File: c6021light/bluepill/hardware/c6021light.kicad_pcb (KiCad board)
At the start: 2 copper layers, 100 x 50 mm, 73 parts, among them J1 Barrel_Jack_Switch, J10 Conn_01x02, J11 Conn_01x02, J12 XpressNet, J2 Conn_01x02, J3 Conn_02x16_Row_Letter_First, J30 Loconet, J4 Conn_01x02, J5 Grove I2C, J50 USB_B_Micro, J51 Conn_01x06, J52 Debug UART, J6 Conn_01x02, J7 Conn_01x02, J8 RJ45, Q30 BC337, U1 L7805, U10 SN75176, U2 L7808, U3 MCP2562, U30 LM393, U4 ISO1050DUB, U50 CH340C

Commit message: wip
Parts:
- removed J2: Conn_01x02, Connector_PinHeader_2.54mm:PinHeader_1x02_P2.54mm_Vertical
- added SW1: SW_Push, w_switch:PCB_PUSH, F.Cu at (136.8, 54.4)
- C51: footprint Capacitor_THT:C_Disc_D5.0mm_W2.5mm_P2.50mm -> Capacitor_SMD:C_0805_2012Metric
- D1, D20, D21: footprint LED_THT:LED_D5.0mm -> LED_THT:LED_D3.0mm
- J51: footprint Connector_PinSocket_2.54mm:PinSocket_1x06_P2.54mm_Vertical -> Connector_PinHeader_2.00mm:PinHeader_1x06_P2.00mm_Vertical
- J52: footprint Connector_PinSocket_2.54mm:PinSocket_1x06_P2.54mm_Vertical -> Connector_PinHeader_2.54mm:PinHeader_1x06_P2.54mm_Vertical
- JP1, JP2: footprint Connector_PinSocket_2.54mm:PinSocket_1x02_P2.54mm_Vertical -> Connector_PinHeader_2.54mm:PinHeader_1x02_P2.54mm_Vertical
- moved J1 98.4 mm to (101.7, 86.4), turned to 270 degrees
- moved C2 95.7 mm to (110.0, 74.9), turned to 180 degrees
- moved C3 91.5 mm to (116.1, 88.3), turned to 270 degrees
- moved C1 90.3 mm to (101.6, 74.9)
- moved D20 88.1 mm to (188.7, 53.7)
- moved C5 87.0 mm to (125.0, 75.9)
- moved U1 86.6 mm to (102.7, 79.9), turned to 0 degrees
- moved U2 78.9 mm to (111.0, 89.9)
- moved D21 77.2 mm to (188.8, 58.5)
- moved J30 76.7 mm to (188.5, 71.6), turned to 90 degrees
- moved R40 75.6 mm to (175.8, 81.2), turned to 90 degrees
- moved R37 72.6 mm to (169.3, 73.5), turned to 270 degrees
- moved C30 62.0 mm to (182.4, 72.8), turned to 180 degrees
- moved R30 60.2 mm to (185.5, 62.0), turned to 270 degrees
- moved JP1 59.1 mm to (143.8, 53.1)
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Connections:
- BP1 pad 10: Net-(BP1-Pad10) -> /M_GO
- BP1 pad 13: /M_GO -> Net-(BP1-Pad13)
- C2 pad 1: Net-(C2-Pad1) -> +5V
- D1 pad 1: Net-(BP1-Pad23) -> Net-(BP1-Pad25)
- J3 pad b1: Net-(J3-Padb1) -> +8V
- J3 pad b11: Net-(J3-Padb11) -> /M_STOP
- J3 pad b12: /M_INIT -> Net-(J3-Padb12)
- J3 pad b13: Net-(J3-Padb13) -> /SCL
- J3 pad b14: +8V -> Net-(J3-Padb14)
- J3 pad b15: Net-(J3-Padb15) -> /SDA
- J3 pad b16: +8V -> Net-(J3-Padb16)
- J3 pad b2: /SDA -> Net-(J3-Padb2)
- J3 pad b3: Net-(J3-Padb3) -> +8V
- J3 pad b4: /SCL -> Net-(J3-Padb4)
- J3 pad b5: Net-(J3-Padb5) -> /M_INIT
- J3 pad b6: /M_STOP -> Net-(J3-Padb6)
- J3 pad b8: /M_GO -> Net-(J3-Padb8)
- J3 pad b9: Net-(J3-Padb9) -> /M_GO
- J4 pad 1: Net-(J3-Padb10) -> Net-(J3-Padb7)
- U1 pad 3: Net-(C2-Pad1) -> +5V
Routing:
- added copper zone on B.Cu, net GND
- added copper zone on F.Cu, net GND
- removed copper zone on B.Cu, net (none)
- removed copper zone on F.Cu, net (none)
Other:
- rule trace_min: 0.2 -> 0.3

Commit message: wip
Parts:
- removed R6: 120, Resistor_THT:R_Axial_DIN0207_L6.3mm_D2.5mm_P7.62mm_Horizontal
- added J2: Conn_02x03_Odd_Even, Connector_PinHeader_2.54mm:PinHeader_2x03_P2.54mm_Vertical, F.Cu at (151.5, 58.2)
- R4: footprint Resistor_THT:R_Axial_DIN0207_L6.3mm_D2.5mm_P7.62mm_Horizontal -> Resistor_THT:R_AXIAL_0_WIRE
- R5: value 0 -> 120
- moved R5 23.6 mm to (115.8, 55.8), turned to 180 degrees
- moved R50 9.96 mm to (177.2, 52.5)
- moved C51 5.23 mm to (184.5, 58.2), turned to 90 degrees
- moved R4 2.96 mm to (119.0, 60.8)
- moved J52 2.42 mm to (160.4, 52.1)
- moved U1 2.17 mm to (104.9, 79.6)
- moved J7 1.73 mm to (114.7, 74.7)
- moved J5 1.66 mm to (136.3, 61.8)
- moved C5 1.28 mm to (124.8, 74.7)
- moved U4 1.28 mm to (119.8, 68.2)
- moved U3 1.28 mm to (124.6, 68.2)
- moved J8 0.54 mm to (102.9, 65.0)
- moved R39 0.38 mm to (152.3, 80.8)
- moved BP1 0.28 mm to (133.0, 84.5)
- moved R34 0.28 mm to (140.1, 80.8)
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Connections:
- R4 pad 1: Net-(R4-Pad1) -> GNDD
- R4 pad 2: +3V3 -> GND
- R5 pad 1: Net-(R5-Pad1) -> Net-(J6-Pad2)
- R5 pad 2: GND -> Net-(J8-Pad8)
- U3 pad 5: Net-(R4-Pad1) -> +3V3
- U3 pad 8: Net-(R5-Pad1) -> GND
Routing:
- net +5V: track 0.00 -> 106.0 mm
- net /CANRX: track 0.00 -> 95.8 mm
- net /CANTX: track 0.00 -> 87.7 mm, vias 0 -> 1
- net /SDA: track 0.00 -> 73.9 mm
- net Net-(D20-Pad1): track 0.00 -> 53.9 mm
- net /SCL: track 0.00 -> 52.9 mm
- net Net-(C31-Pad1): track 0.36 -> 47.5 mm, vias 0 -> 1
- net Net-(Q30-Pad1): track 0.00 -> 44.7 mm
- net /RxD: track 0.00 -> 43.6 mm, vias 0 -> 2
- net Net-(D21-Pad1): track 0.00 -> 40.2 mm
- net +5VD: track 0.00 -> 36.1 mm
- net /TxD: track 0.00 -> 34.2 mm, vias 0 -> 4
- net /RS485ENA: track 0.00 -> 33.7 mm, vias 0 -> 2
- net /LN_TX: track 0.00 -> 30.4 mm
- net +12V: track 0.00 -> 30.3 mm
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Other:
- net class Default: trace_width 0.25 -> 0.3
- net class Double added: clearance 0.2, trace_width 0.6, via_dia 0.8, via_drill 0.4

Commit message: close to first release
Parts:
- added REF**: Symbol_CreativeCommons_CopperTop_Type2_Small, Symbol:Symbol_CreativeCommons_CopperTop_Type2_Small, F.Cu at (118.7, 77.3)
- added TP1: Conn_01x01, TestPoint:Test_Point_NA, F.Cu at (101.2, 80.8)
- added TP2: Conn_01x01, TestPoint:Test_Point_NA, F.Cu at (111.0, 87.4)
- C1, C2, C30, C31: footprint Capacitor_THT:C_Disc_D5.0mm_W2.5mm_P2.50mm -> Capacitor_THT:C_Disc_D3.0mm_W1.6mm_P2.50mm
- C10: footprint Capacitor_THT:C_Disc_D5.0mm_W2.5mm_P2.50mm -> Capacitor_THT:C_Disc_D3.0mm_W2.0mm_P2.50mm
- J2: value Conn_02x03_Odd_Even -> Conn_02x04_Odd_Even; footprint Connector_PinHeader_2.54mm:PinHeader_2x03_P2.54mm_Vertical -> Connector_PinHeader_2.54mm:PinHeader_2x04_P2.54mm_Vertical
- J8: footprint w_conn_misc:8p8c -> w_conn_pc:mebp8
- moved C51 14.4 mm to (170.8, 62.4)
- moved C7 9.34 mm to (124.8, 62.2)
- moved C50 5.16 mm to (183.2, 58.9)
- moved R51 3.89 mm to (185.9, 58.4)
- moved J2 3.84 mm to (151.1, 62.0)
- moved C10 3.24 mm to (185.0, 87.7), turned to 90 degrees
- moved C1 2.80 mm to (104.1, 76.2), turned to 180 degrees
- moved J4 2.57 mm to (128.5, 86.4), turned to 180 degrees
- moved J52 2.25 mm to (158.2, 51.8)
- moved U50 1.97 mm to (175.4, 58.8)
- moved C52 1.80 mm to (180.5, 58.5)
- moved U1 1.62 mm to (103.8, 80.8)
- moved C2 1.33 mm to (110.4, 76.2)
- moved J8 1.09 mm to (102.5, 66.0)
- moved J50 0.74 mm to (183.6, 53.5)
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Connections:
- J2 pad 1: Net-(BP1-Pad30) -> Net-(BP1-Pad31)
- J2 pad 2: Net-(BP1-Pad31) -> Net-(BP1-Pad32)
- J2 pad 3: Net-(BP1-Pad29) -> Net-(BP1-Pad30)
- J2 pad 4: Net-(BP1-Pad32) -> Net-(BP1-Pad33)
- J2 pad 5: GND -> Net-(BP1-Pad29)
- J2 pad 6: +3V3 -> Net-(BP1-Pad34)
- J8 pad : (no net) -> GNDD
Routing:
- net GND: track 0.89 -> 140.9 mm, vias 0 -> 19
- net +5V: track 106.0 -> 214.3 mm
- net +3V3: track 2.90 -> 88.0 mm, vias 0 -> 1
- net Net-(BP1-Pad23): track 0.00 -> 66.9 mm, vias 0 -> 4
- net +8V: track 0.00 -> 62.7 mm, vias 0 -> 2
- net +12V: track 30.3 -> 92.0 mm
- net /RS485TxD: track 0.18 -> 40.2 mm, vias 0 -> 1
- net /SCL: track 52.9 -> 92.9 mm, vias 0 -> 2
- net Net-(R12-Pad1): track 0.00 -> 39.5 mm, vias 0 -> 5
- net /TxD: track 34.2 -> 72.6 mm
- net Net-(J11-Pad2): track 0.00 -> 37.5 mm
- net /SDA: track 73.9 -> 107.2 mm
- net /M_STOP: track 0.00 -> 27.5 mm
- net Net-(J3-Padb7): track 0.00 -> 27.4 mm, vias 0 -> 1
- net /SDA2: track 0.00 -> 26.5 mm, vias 0 -> 2
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- added copper zone on B.Cu, net GNDD
- added copper zone on F.Cu, net GNDD
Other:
- board text added: "3V3 GND"
- board text added: "CAN 18V"
- board text added: "DTR"
- board text added: "Damian Philpp 2020/06 Gerhard Bertrelsmann"
- board text added: "Loconet"
- board text added: "Loconet 12V"
- board text added: "RX"
- board text added: "TX"

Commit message: closer to V1.0
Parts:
- moved JP1 0.46 mm to (144.0, 53.5)
- moved R13 0.18 mm to (191.4, 98.9)
- moved R14 0.13 mm to (188.2, 91.3)
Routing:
- net Net-(J10-Pad1): track 20.1 -> 21.0 mm

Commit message: more fixes
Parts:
- added J31: Conn_01x02, Connector_PinHeader_2.54mm:PinHeader_1x02_P2.54mm_Vertical, F.Cu at (187.2, 56.9)
- added Q31: BC547, Package_TO_SOT_THT:TO-92_Inline, F.Cu at (196.0, 59.2)
- added Q32: BC547, Package_TO_SOT_THT:TO-92_Inline, F.Cu at (190.5, 59.2)
- added R41: 47, w_pth_resistors:RC03, F.Cu at (188.1, 53.6)
- added R42: 10k, w_pth_resistors:RC03, F.Cu at (188.1, 51.6)
- C3, C32, C4, C5, C6, C7, C8: footprint Capacitor_THT:C_Disc_D5.0mm_W2.5mm_P2.50mm -> Capacitor_THT:C_Disc_D3.0mm_W1.6mm_P2.50mm
- C50, C51, C52, J50, R50, R51, U50: moved to B.Cu
- J51: footprint Connector_PinHeader_2.00mm:PinHeader_1x06_P2.00mm_Vertical -> Connector_PinHeader_1.27mm:PinHeader_1x06_P1.27mm_Vertical
- R13, R14, R15: footprint Resistor_THT:R_Axial_DIN0207_L6.3mm_D2.5mm_P7.62mm_Horizontal -> w_pth_resistors:RC03
- moved J11 50.7 mm to (112.4, 84.8)
- moved R15 23.6 mm to (190.3, 95.0), turned to 270 degrees
- moved D20 12.9 mm to (181.2, 63.9)
- moved C50 12.3 mm to (171.8, 54.5), turned to 0 degrees
- moved J51 9.49 mm to (168.3, 64.5), turned to 180 degrees
- moved D21 8.11 mm to (181.2, 59.4)
- moved R50 7.54 mm to (182.6, 56.6)
- moved C51 7.51 mm to (168.1, 55.4), turned to 180 degrees
- moved R51 7.20 mm to (178.7, 58.1)
- moved R30 5.61 mm to (185.2, 67.8)
- moved R31 5.59 mm to (185.2, 77.6)
- moved C52 5.20 mm to (178.5, 63.3), turned to 270 degrees
- moved J50 5.14 mm to (178.5, 52.9), turned to 0 degrees
- moved R13 4.13 mm to (192.5, 94.9), turned to 270 degrees
- moved R14 3.66 mm to (188.2, 95.0)
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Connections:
- net Net-(J30-Pad3) renamed /LN
- J8 pad : GNDD -> (no net)
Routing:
- net +12V: track 92.0 -> 173.3 mm
- net Net-(J11-Pad2): track 37.5 -> 101.0 mm, vias 0 -> 4
- net GND: track 140.9 -> 176.0 mm, vias 19 -> 18
- net Net-(Q31-Pad3): track 0.00 -> 20.7 mm, vias 0 -> 1
- net Net-(J31-Pad1): track 0.00 -> 17.6 mm, vias 0 -> 1
- net Net-(Q31-Pad2): track 0.00 -> 17.4 mm
- net (no net): track 0.00 -> 15.5 mm
- net GNDD: track 21.0 -> 5.86 mm
- net Net-(D20-Pad1): track 54.2 -> 41.5 mm
- net /LN: track 11.3 -> 22.4 mm
- net /CTS: track 8.60 -> 17.0 mm
- net Net-(J50-Pad2): track 8.12 -> 16.3 mm, vias 0 -> 2
- net Net-(J10-Pad2): track 12.0 -> 5.95 mm
- net /DTR: track 23.4 -> 17.7 mm
- net Net-(J51-Pad6): track 8.36 -> 3.02 mm, vias 1 -> 0
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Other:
- board text added: "Damian Philip 2020/06 Gerhard Bertelsmann"
- board text added: "GND"
- board text added: "Pullup"
- board text added: "RS485 12V"
- board text added: "RS485 Xpressnet"
- board text removed: "Damian Philpp 2020/06 Gerhard Bertrelsmann"
- board text removed: "Loconet 12V"

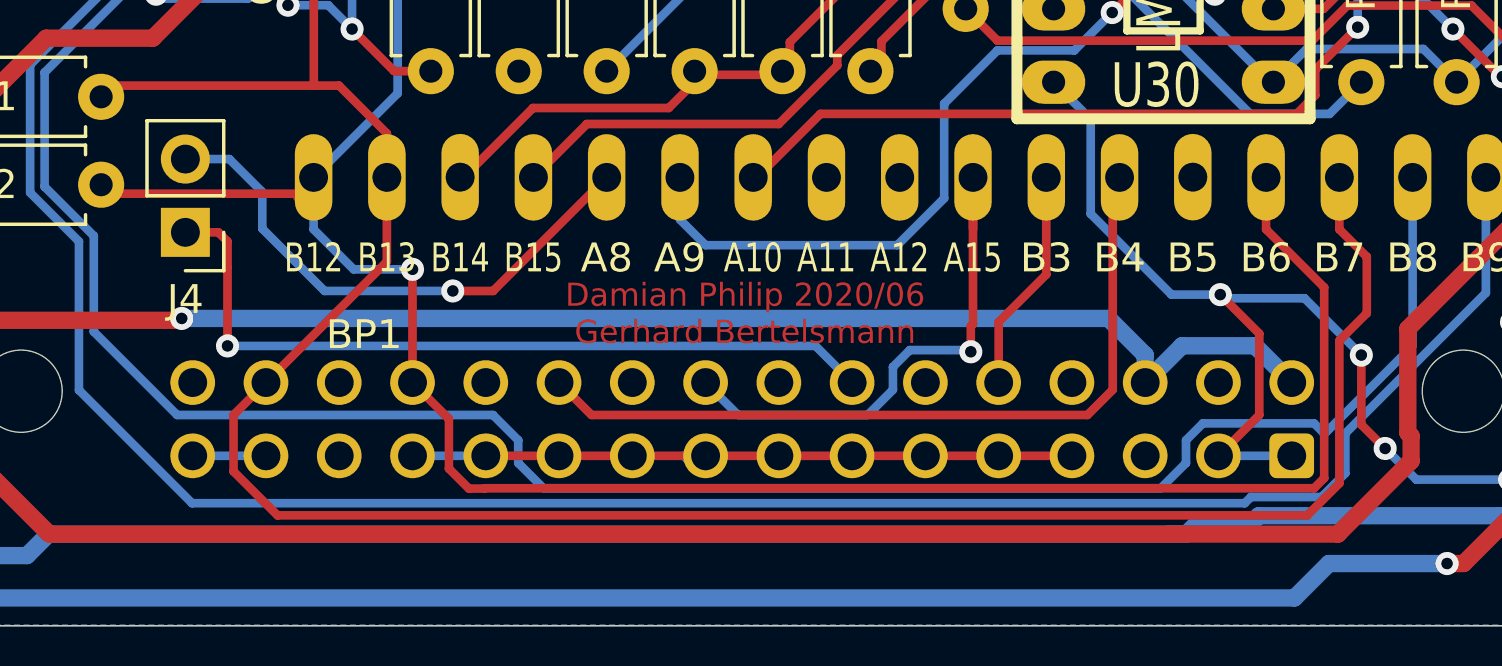
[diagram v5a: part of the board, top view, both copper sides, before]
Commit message: fix DIN socket
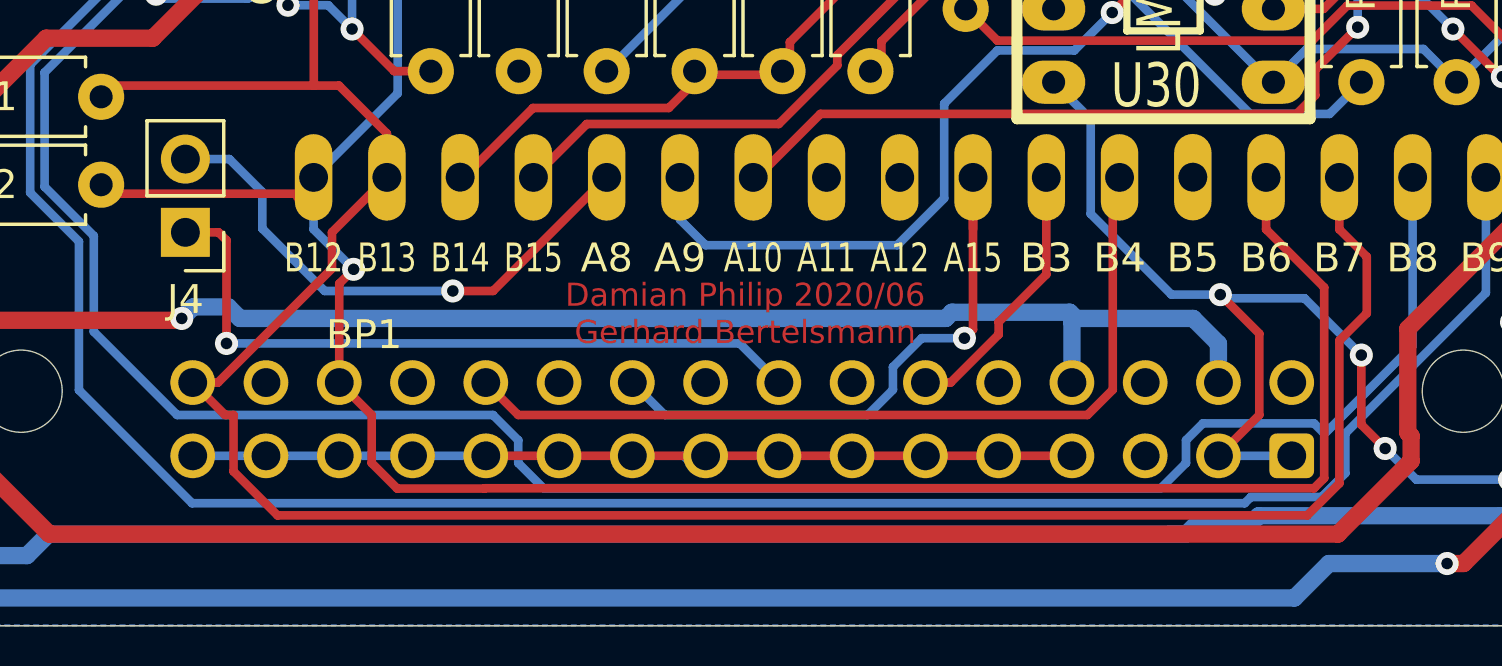
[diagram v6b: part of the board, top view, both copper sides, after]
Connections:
- J3 pad b1: +8V -> Net-(J3-Padb1)
- J3 pad b10: Net-(J3-Padb10) -> /M_GO
- J3 pad b11: /M_STOP -> Net-(J3-Padb11)
- J3 pad b12: Net-(J3-Padb12) -> /M_STOP
- J3 pad b13: /SCL -> Net-(J3-Padb13)
- J3 pad b14: Net-(J3-Padb14) -> /SCL
- J3 pad b15: /SDA -> Net-(J3-Padb15)
- J3 pad b16: Net-(J3-Padb16) -> /SDA
- J3 pad b2: Net-(J3-Padb2) -> +8V
- J3 pad b3: +8V -> Net-(J3-Padb3)
- J3 pad b4: Net-(J3-Padb4) -> +8V
- J3 pad b5: /M_INIT -> Net-(J3-Padb5)
- J3 pad b6: Net-(J3-Padb6) -> /M_INIT
- J3 pad b9: /M_GO -> Net-(J3-Padb9)
- J4 pad 1: Net-(J3-Padb7) -> Net-(J3-Padb8)
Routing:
- net Net-(J3-Padb7): track 27.4 -> 0.00 mm, vias 1 -> 0
- net Net-(J3-Padb8): track 0.44 -> 25.3 mm, vias 0 -> 1
- net GND: track 176.0 -> 181.1 mm
- net /M_STOP: track 27.5 -> 30.0 mm
- net /M_GO: track 19.0 -> 21.0 mm
- net /SDA: track 107.3 -> 109.3 mm
- net /M_INIT: track 7.80 -> 9.36 mm
- net /SCL: track 92.9 -> 93.6 mm
- net +8V: track 62.7 -> 62.1 mm

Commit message: fix name
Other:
- board text added: "Damian Philipp 2020/06 Gerhard Bertelsmann"
- board text removed: "Damian Philip 2020/06 Gerhard Bertelsmann"

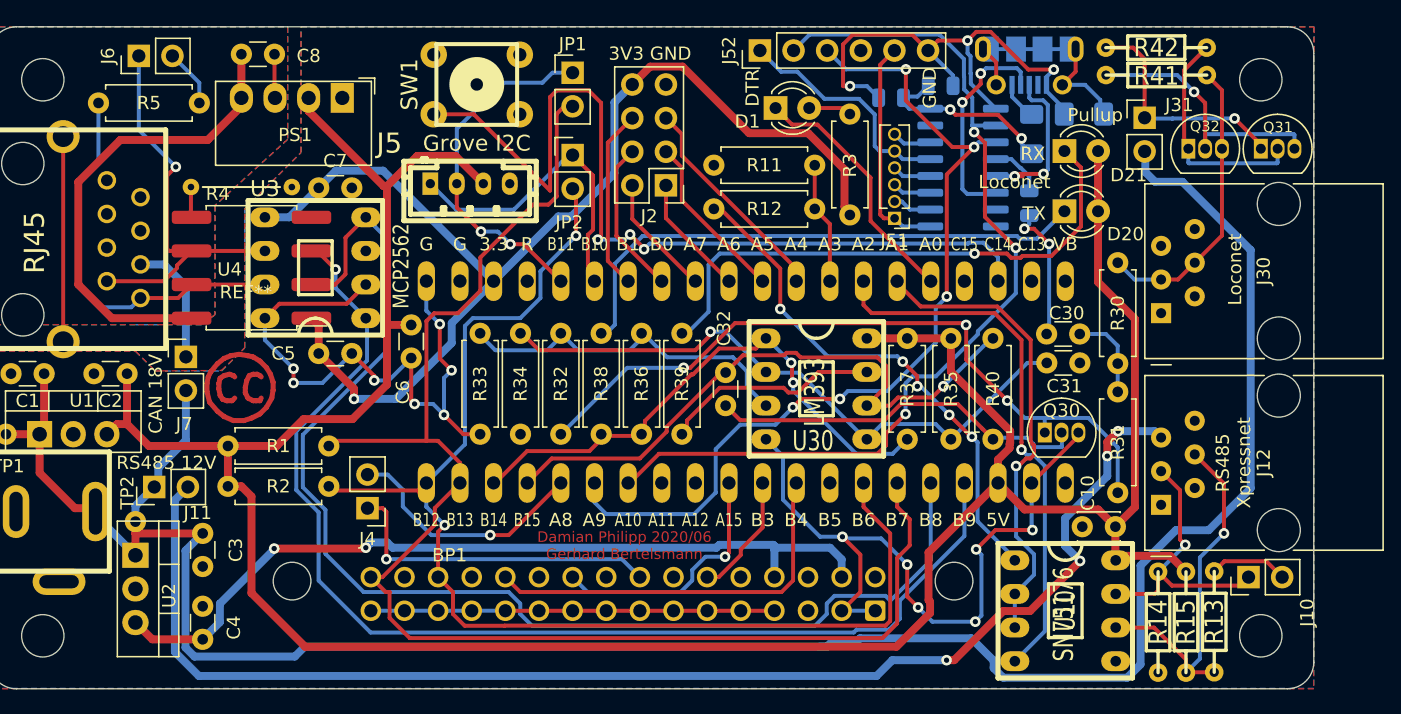
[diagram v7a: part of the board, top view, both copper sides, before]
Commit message: move&add some references - looks better
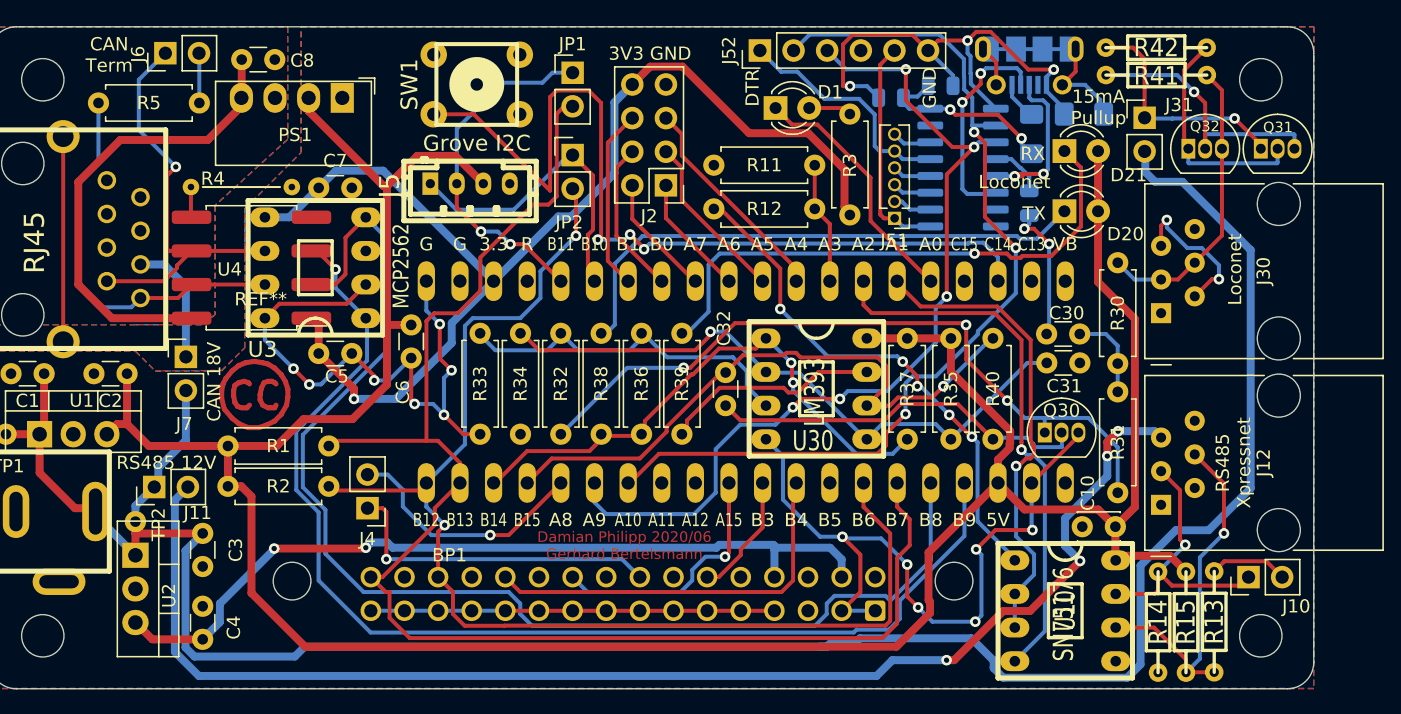
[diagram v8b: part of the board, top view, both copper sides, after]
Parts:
- moved J6 2.02 mm to (113.3, 52.0)
- moved REF** 1.24 mm to (119.9, 77.9)
- moved C8 0.41 mm to (119.0, 52.5)
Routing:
- net GND: track 181.1 -> 191.8 mm, vias 18 -> 20
- net GNDD: track 5.86 -> 2.60 mm
- net Net-(J6-Pad1): track 30.9 -> 32.0 mm
- net Net-(J6-Pad2): track 4.27 -> 3.77 mm
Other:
- board text added: "15mA Pullup"
- board text added: "CAN Term"
- board text removed: "Pullup"
